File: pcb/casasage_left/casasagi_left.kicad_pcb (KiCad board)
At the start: 2 copper layers, 133.3 x 83.7 mm, 113 parts, among them J1 USB_C_Receptacle_USB2.0, J2 AudioJack4, J3 Conn_01x05, SW1 RESET, SW2 BOOT, U1 TLV73333PDBV, U2 STM32F072C8Tx, U3 AT24CS32-XHM, Y1 8MHz

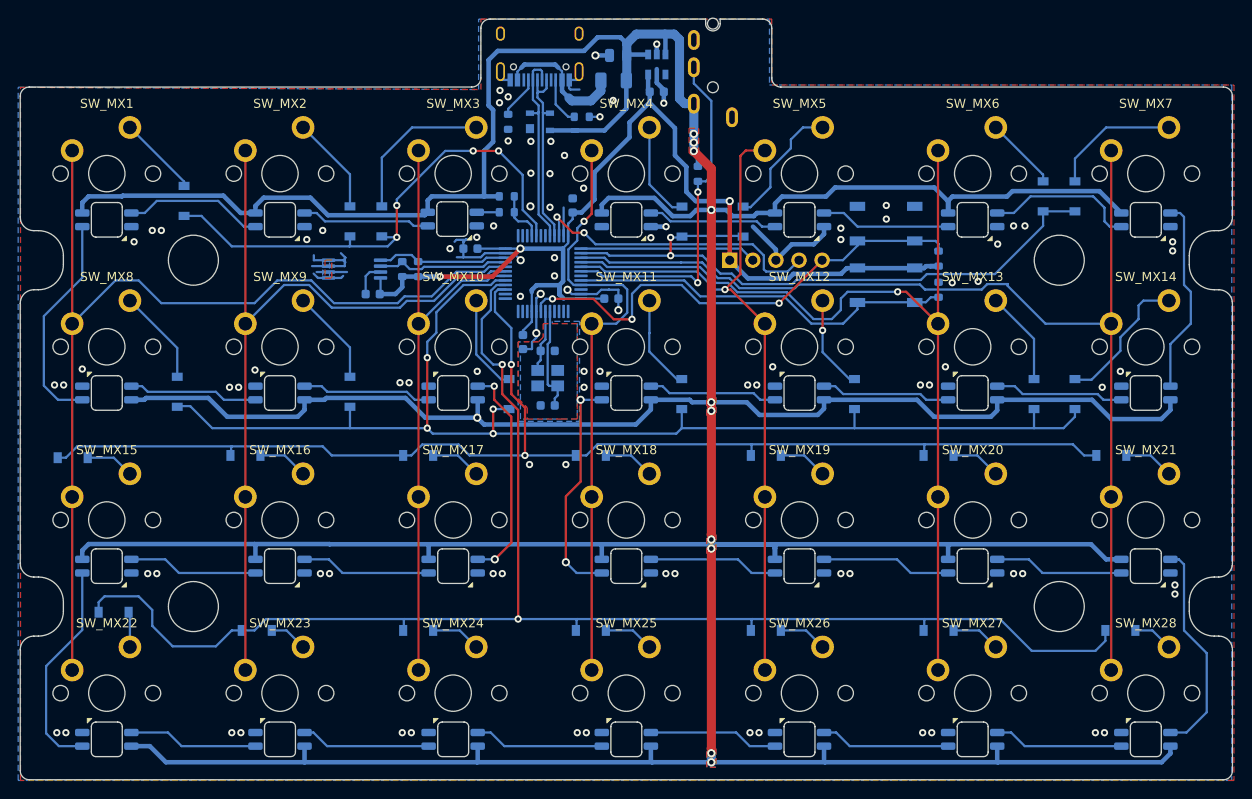
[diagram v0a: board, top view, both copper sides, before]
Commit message: correct tab and connectors dimention
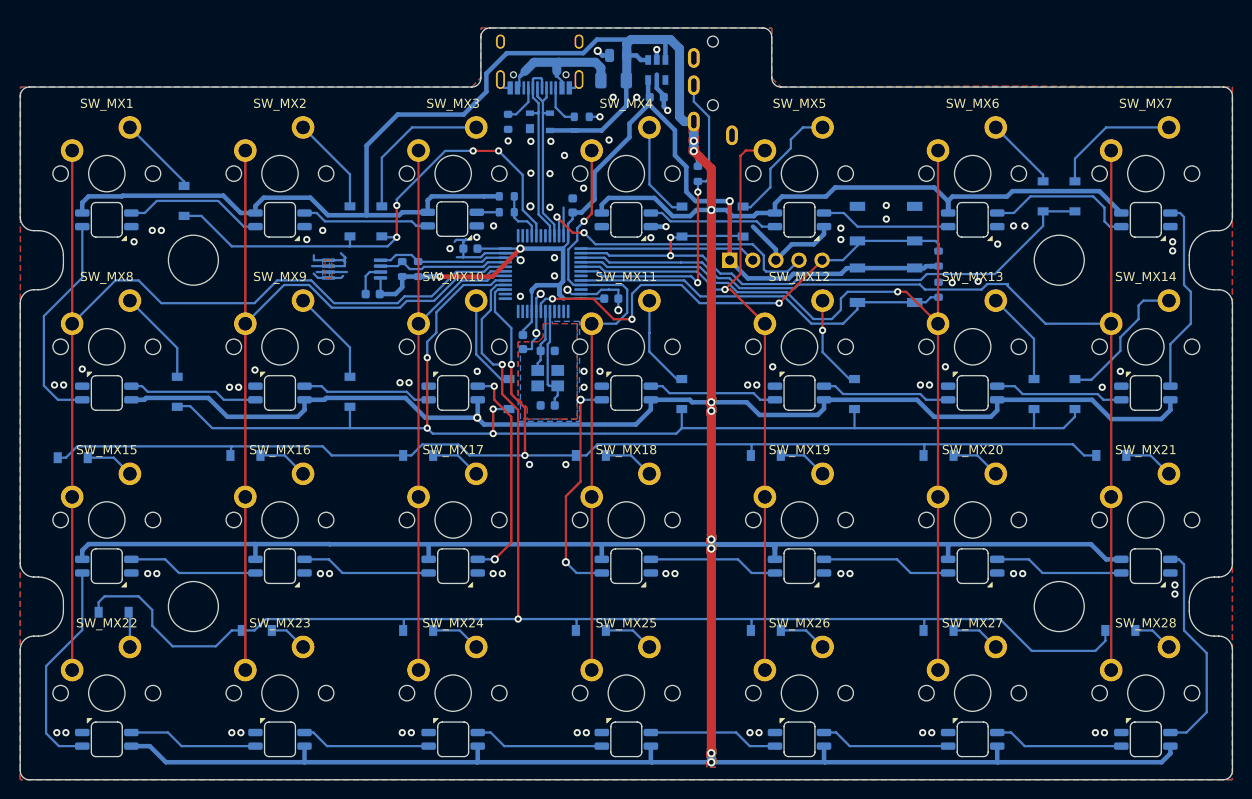
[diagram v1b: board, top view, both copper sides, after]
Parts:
- moved J2 1.98 mm to (116.7, 34.0)
- moved J1 0.88 mm to (97.6, 36.5)
- moved C2 0.60 mm to (110.5, 41.6)
- moved U1 0.60 mm to (110.5, 38.6)
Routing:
- net +5V: track 655.8 -> 662.2 mm, vias 11 -> 10
- net /SPLIT_DATA: track 39.0 -> 36.8 mm
- net GND: track 77.9 -> 75.9 mm, vias 96 -> 95
- net /USB_D+: track 20.9 -> 19.5 mm
- net /USB_D-: track 22.0 -> 21.0 mm
- net +3V3: track 120.8 -> 120.0 mm
- net Net-(F1-Pad2): track 14.9 -> 15.7 mm
- net Net-(J1-PadB5): track 5.30 -> 4.63 mm
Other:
- board size 133.3 x 83.7 mm -> 133.3 x 82.7 mm

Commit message: make switch matrix simple
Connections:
- D10 pad 1: /ROW2 -> /ROW1
- D11 pad 1: /ROW2 -> /ROW1
- D12 pad 1: /ROW2 -> /ROW1
- D13 pad 1: /ROW2 -> /ROW1
- D14 pad 1: /ROW2 -> /ROW1
- D15 pad 1: /ROW2 -> /ROW1
- D16 pad 1: /ROW3 -> /ROW2
- D17 pad 1: /ROW3 -> /ROW2
- D18 pad 1: /ROW3 -> /ROW2
- D19 pad 1: /ROW3 -> /ROW2
- D20 pad 1: /ROW3 -> /ROW2
- D21 pad 1: /ROW3 -> /ROW2
- D22 pad 1: /ROW3 -> /ROW2
- D23 pad 1: /ROW4 -> /ROW3
- D24 pad 1: /ROW4 -> /ROW3
- D25 pad 1: /ROW4 -> /ROW3
- D26 pad 1: /ROW4 -> /ROW3
- D27 pad 1: /ROW4 -> /ROW3
- D28 pad 1: /ROW4 -> /ROW3
- D29 pad 1: /ROW4 -> /ROW3
- D5 pad 1: /ROW1 -> /ROW0
- D6 pad 1: /ROW1 -> /ROW0
- D7 pad 1: /ROW1 -> /ROW0
- D8 pad 1: /ROW1 -> /ROW0
- D9 pad 1: /ROW2 -> /ROW1
- U2 pad 15: /ROW3 -> /ROW2
- U2 pad 16: /ROW4 -> /ROW3
- U2 pad 17: /ROW2 -> /ROW1
- U2 pad 29: /ROW0 -> (no net)
- U2 pad 38: /ROW1 -> /ROW0
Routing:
- net /ROW4: track 165.5 -> 0.00 mm, vias 2 -> 0
- net /ROW0: track 56.6 -> 164.3 mm, vias 4 -> 5
- net /ROW1: track 70.0 -> 138.1 mm, vias 2 -> 4
- net /ROW3: track 141.3 -> 165.5 mm
- net /ROW2: track 137.3 -> 141.3 mm, vias 4 -> 2
- net GND: track 75.9 -> 72.9 mm, vias 95 -> 94
- net Net-(LED20-Pad2): track 25.3 -> 24.3 mm

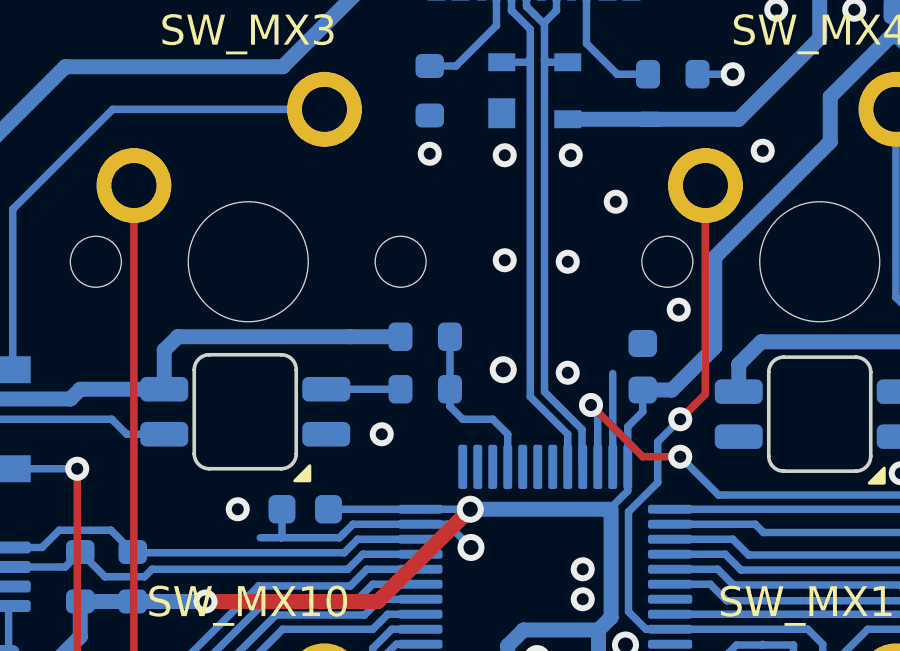
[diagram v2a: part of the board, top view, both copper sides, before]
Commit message: add handness resistor
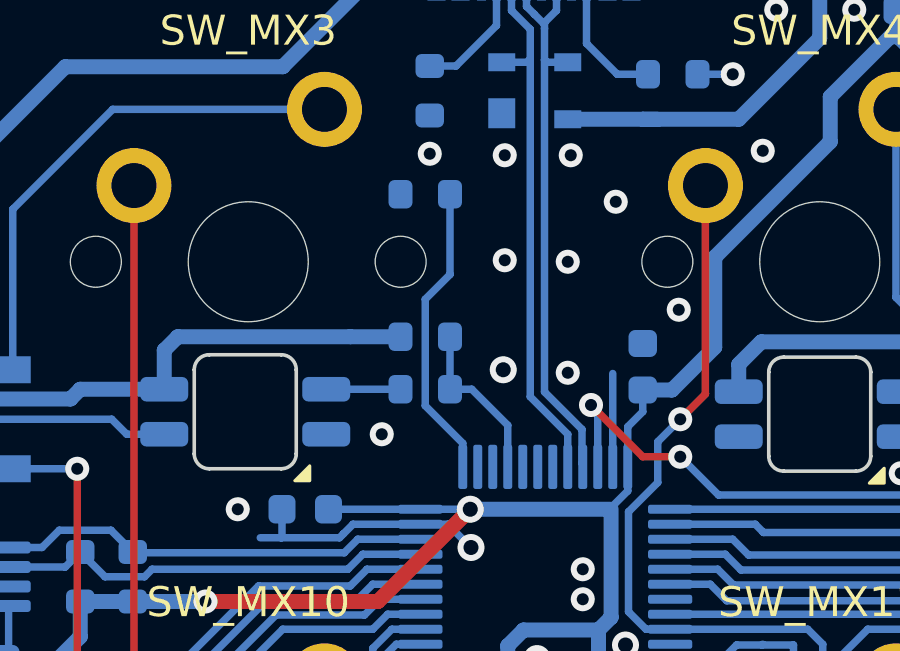
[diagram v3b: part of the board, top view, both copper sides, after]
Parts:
- added R10: DNP, Resistor_SMD:R_0603_1608Metric, B.Cu at (94.0, 47.8)
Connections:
- U2 pad 25: (no net) -> Net-(R10-Pad1)
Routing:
- net Net-(R10-Pad1): track 0.00 -> 9.95 mm

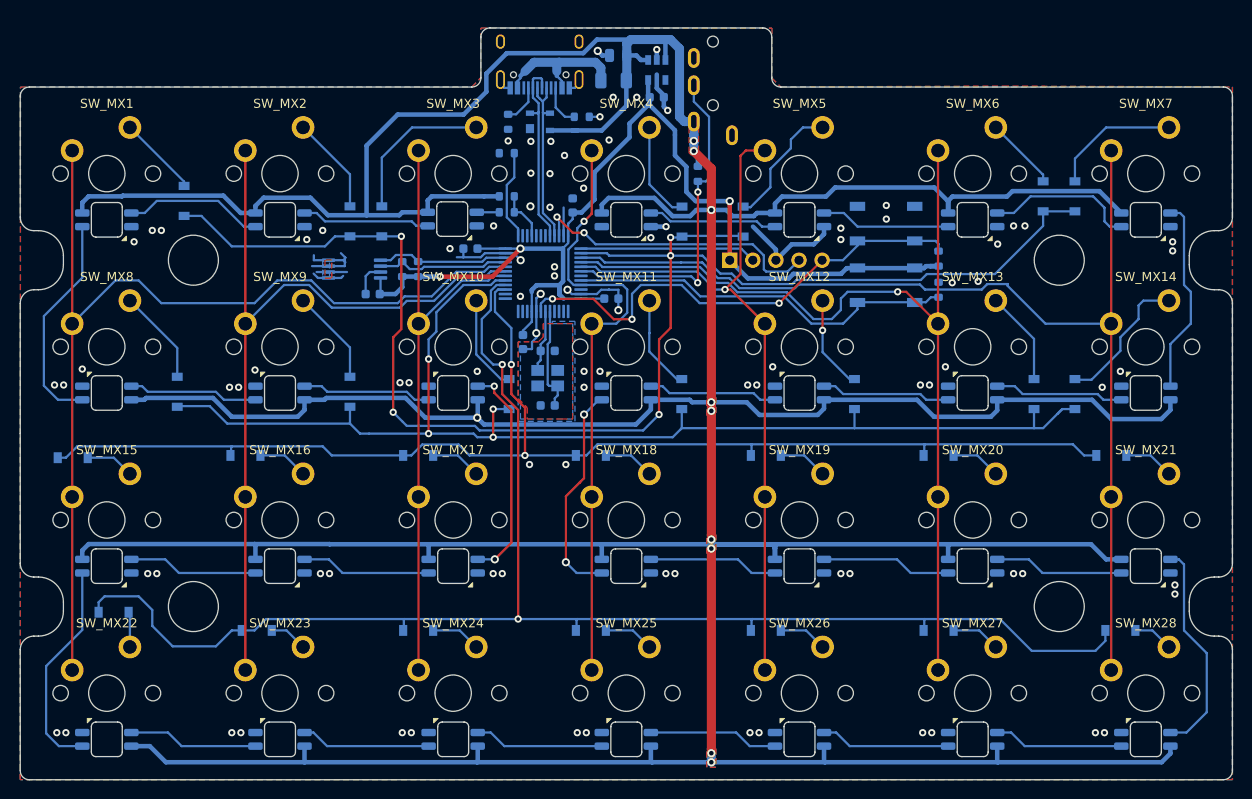
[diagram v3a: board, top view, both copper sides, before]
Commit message: adjust traces and silks
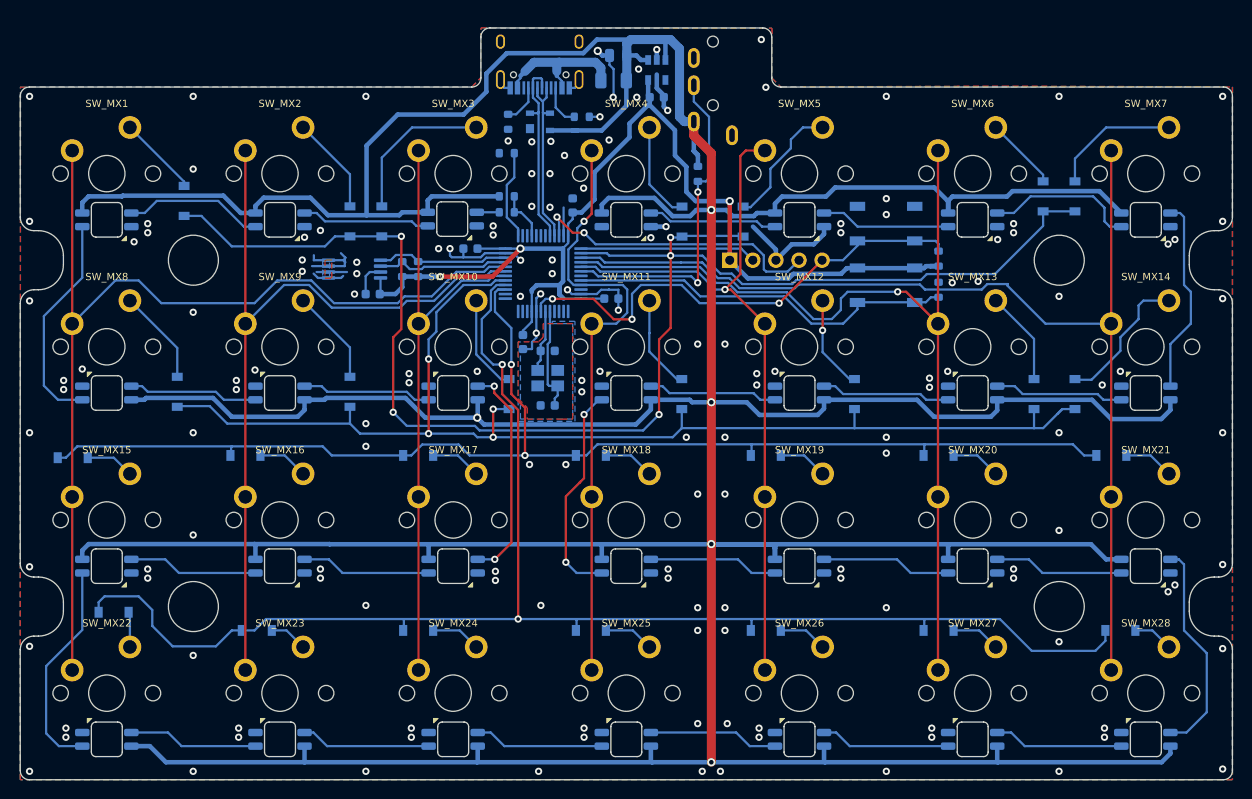
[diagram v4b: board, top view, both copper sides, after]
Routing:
- net GND: track 72.9 -> 79.3 mm, vias 94 -> 157
- net +5V: track 662.2 -> 664.0 mm, vias 10 -> 5
- removed copper zone on B.Cu, net +5V
- removed copper zone on F.Cu, net +5V

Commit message: update reference number for panelization
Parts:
- renumbered C1 to C101, C2 to C102, C9 to C103, C7 to C104, C3 to C105, C4 to C106, C5 to C107, C6 to C108, C8 to C109, D1 to D101, D2 to D102, D3 to D103, D4 to D104, D5 to D105, D6 to D106, D7 to D107, D8 to D108, D9 to D109, D10 to D110, D11 to D111, D12 to D112, D13 to D113, D14 to D114, D15 to D115, D16 to D116, D17 to D117, D18 to D118, D19 to D119, D20 to D120, D21 to D121, D22 to D122, D23 to D123, D24 to D124, D25 to D125, D26 to D126, D27 to D127, D28 to D128, D29 to D129, F1 to F101, J1 to J101, J2 to J102, J3 to J103, LED1 to LED101, LED2 to LED102, LED3 to LED103, LED4 to LED104, LED5 to LED105, LED6 to LED106, LED7 to LED107, LED8 to LED108, LED9 to LED109, LED10 to LED110, LED11 to LED111, LED12 to LED112, LED13 to LED113, LED14 to LED114, LED15 to LED115, LED16 to LED116, LED17 to LED117, LED18 to LED118, LED19 to LED119, LED20 to LED120, LED21 to LED121, LED22 to LED122, LED23 to LED123, LED24 to LED124, LED25 to LED125, LED26 to LED126, LED27 to LED127, LED28 to LED128, R1 to R101, R2 to R102, R6 to R103, R7 to R104, R3 to R105, R4 to R106, R9 to R107, R5 to R108, R10 to R109, R8 to R110, SW1 to SW101, SW2 to SW102, SW_MX1 to SW_MX101, SW_MX2 to SW_MX102, SW_MX3 to SW_MX103, SW_MX4 to SW_MX104, SW_MX5 to SW_MX105, SW_MX6 to SW_MX106, SW_MX7 to SW_MX107, SW_MX8 to SW_MX108, SW_MX9 to SW_MX109, SW_MX10 to SW_MX110, SW_MX11 to SW_MX111, SW_MX12 to SW_MX112, SW_MX13 to SW_MX113, SW_MX14 to SW_MX114, SW_MX15 to SW_MX115, SW_MX16 to SW_MX116, SW_MX17 to SW_MX117, SW_MX18 to SW_MX118, SW_MX19 to SW_MX119, SW_MX20 to SW_MX120, SW_MX21 to SW_MX121, SW_MX22 to SW_MX122, SW_MX23 to SW_MX123, SW_MX24 to SW_MX124, SW_MX25 to SW_MX125, SW_MX26 to SW_MX126, SW_MX27 to SW_MX127, SW_MX28 to SW_MX128, U1 to U101, U3 to U102, U2 to U103, Y1 to Y101

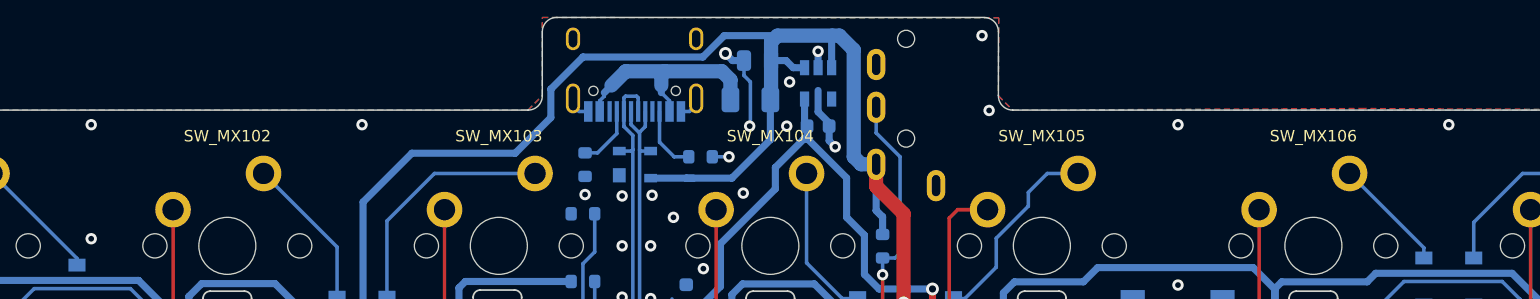
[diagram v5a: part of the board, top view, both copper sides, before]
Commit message: add copyright on pcbs
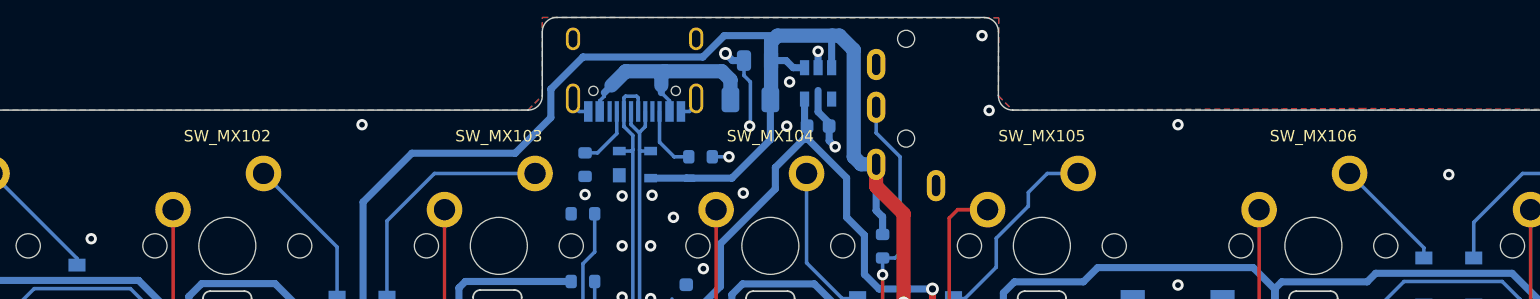
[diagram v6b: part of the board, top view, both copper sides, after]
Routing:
- net GND: vias 157 -> 156
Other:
- board text added: "(c) 2020, SMKiJ Casasagi Contributors"
- board text added: "Casasagi Left PCB / Rev. Alpha"

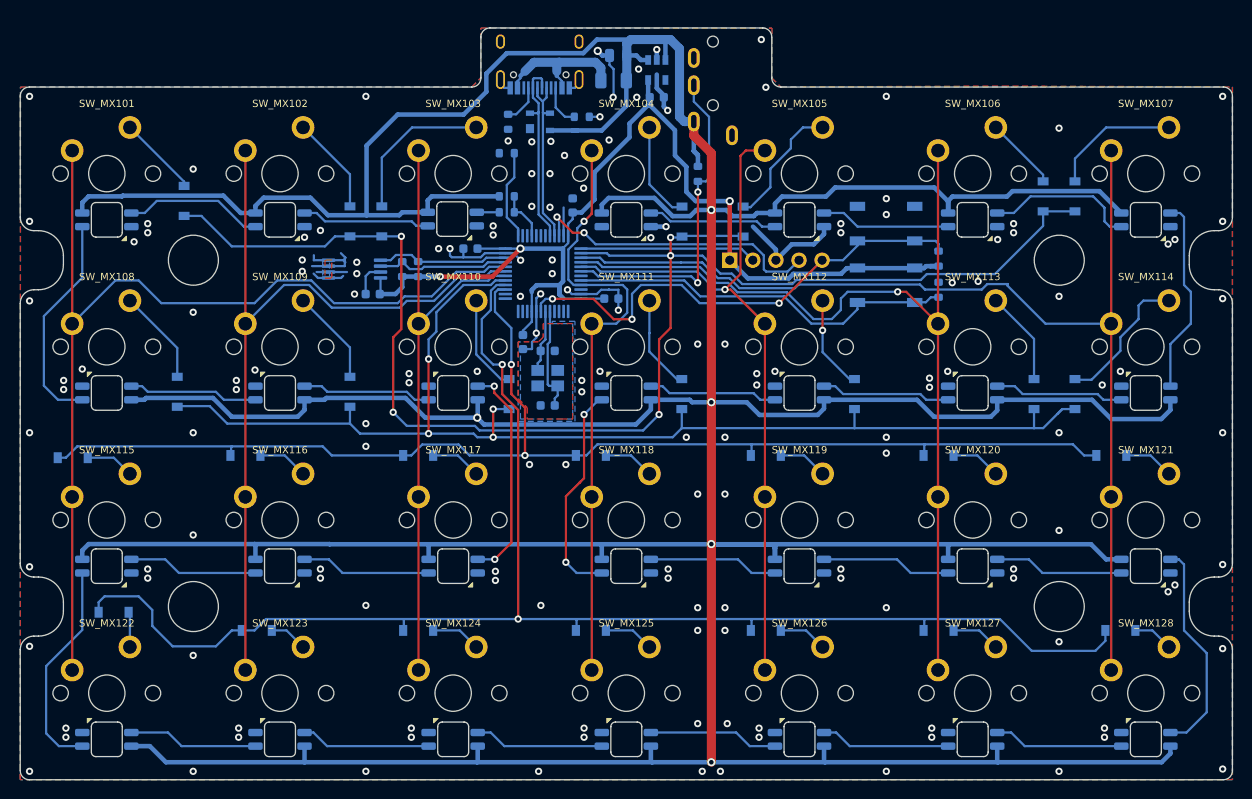
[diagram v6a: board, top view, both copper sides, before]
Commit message: add teardrop and adjust trace
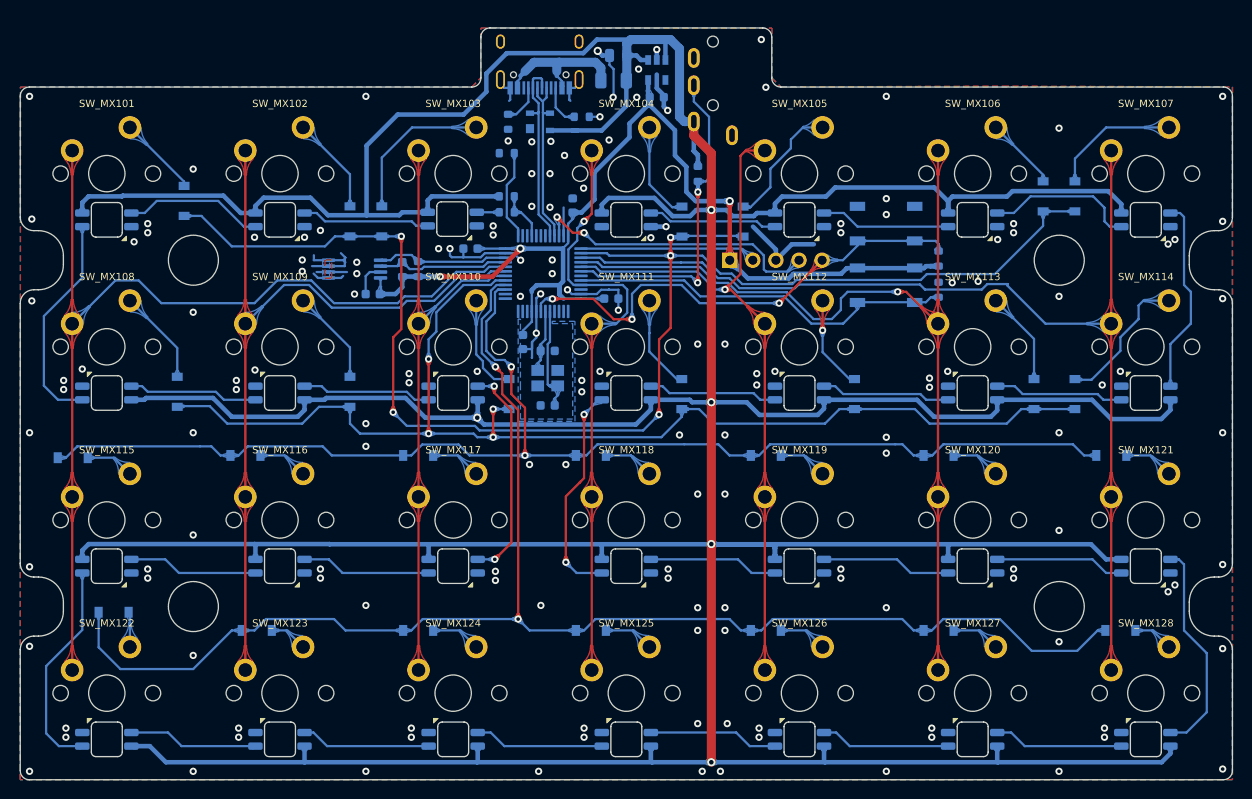
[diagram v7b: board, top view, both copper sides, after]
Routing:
- net /ROW1: track 138.1 -> 135.0 mm
- net GND: track 79.3 -> 81.6 mm, vias 156 -> 157
- net /ROW3: track 165.5 -> 164.4 mm
- net /ROW2: track 141.3 -> 142.0 mm
- net +5V: track 664.0 -> 664.6 mm
